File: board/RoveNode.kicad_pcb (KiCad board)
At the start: 4 copper layers, 25.4 x 61 mm, 60 parts, among them J1 Conn_01x05, J3 Conn_01x24_Pin, J4 Conn_01x24_Pin, SW1 RST_Push, SW2 BOOT_Push, U1 STM32H563RITx, U2 AP63203WU-7, U3 SN65HVD232, U4 LAN8742A, U5 USBLC6-4SC6, X1 NX2016SA-25.000M-STD-CZS-1

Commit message: Layout Complete
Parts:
- C1, C10, C11, C13, C14, C15, C16, C19, C20, C3, C30, C31, C32, C33, C34, C35, C4, C7, C8, C9, FB1, R16, R23: moved to B.Cu
- J1: footprint Connector_PinSocket_2.54mm:PinSocket_1x05_P2.54mm_Vertical -> Connector_JST:JST_PH_S5B-PH-K_1x05_P2.00mm_Horizontal
- moved D3 85.4 mm to (123.2, 65.0)
- moved C7 84.4 mm to (131.1, 87.4), turned to 180 degrees
- moved C8 84.2 mm to (131.1, 89.5), turned to 180 degrees
- moved C13 84.1 mm to (127.8, 76.2)
- moved C4 84.0 mm to (127.8, 70.1), turned to 180 degrees
- moved C19 83.9 mm to (127.8, 78.2)
- moved C9 83.9 mm to (131.1, 91.4), turned to 180 degrees
- moved C10 83.6 mm to (131.1, 93.5), turned to 180 degrees
- moved C11 83.4 mm to (131.1, 95.5), turned to 180 degrees
- moved C14 83.1 mm to (131.1, 97.5), turned to 180 degrees
- moved C16 82.7 mm to (125.7, 61.5)
- moved R15 82.1 mm to (131.1, 51.3), turned to 90 degrees
- moved C20 79.8 mm to (127.8, 72.1)
- moved C30 79.8 mm to (127.8, 74.2)
- moved C32 76.1 mm to (124.0, 80.3), turned to 180 degrees
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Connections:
- J3 pad 10: PB7 -> PC15
- J3 pad 11: PB8 -> PH0
- J3 pad 12: PC13 -> PH1
- J3 pad 13: PC14 -> PC2
- J3 pad 14: PC15 -> PC3
- J3 pad 15: PH0 -> PA0
- J3 pad 16: PH1 -> PA3
- J3 pad 17: PC2 -> PA4
- J3 pad 18: PC3 -> PA6
- J3 pad 19: PA0 -> PB0
- J3 pad 2: PA15 -> PD2
- J3 pad 20: PA3 -> PB1
- J3 pad 21: PA4 -> PB2
- J3 pad 22: PA6 -> PB10
- J3 pad 3: PC10 -> PB4
- J3 pad 4: PC11 -> PB5
- J3 pad 5: PC12 -> PB6
- J3 pad 6: PD2 -> PB7
- J3 pad 7: PB4 -> PB8
- J3 pad 8: PB5 -> PC13
- J3 pad 9: PB6 -> PC14
- J4 pad 10: PC8 -> PA10
- J4 pad 11: PC7 -> PA9
- J4 pad 12: PC6 -> PA8
- J4 pad 13: TX- -> PC9
- J4 pad 14: PB14 -> PC8
- J4 pad 15: PB13 -> PC7
- J4 pad 16: TX+ -> PC6
- J4 pad 17: PB10 -> PB14
- J4 pad 18: PB2 -> PB13
- J4 pad 19: PB1 -> RX+
- J4 pad 20: PB0 -> RX-
- J4 pad 21: RX- -> TX+
- J4 pad 22: RX+ -> TX-
- J4 pad 23: LED1 -> LED2
- J4 pad 24: LED2 -> LED1
- J4 pad 4: CAN_H -> CAN_L
- J4 pad 5: CAN_L -> CAN_H
- J4 pad 6: PA10 -> PC12
- J4 pad 7: PA9 -> PC11
- J4 pad 8: PA8 -> PC10
- J4 pad 9: PC9 -> PA15
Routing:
- net VIN: track 0.00 -> 82.5 mm, vias 0 -> 3
- net GND: track 7.94 -> 62.9 mm, vias 6 -> 80
- net PD2: track 0.00 -> 39.2 mm, vias 0 -> 1
- net SWDIO: track 0.00 -> 36.4 mm, vias 0 -> 1
- net CAN_TX: track 0.00 -> 35.3 mm, vias 0 -> 2
- net PB4: track 0.00 -> 34.9 mm, vias 0 -> 1
- net SWDCLK: track 1.49 -> 36.4 mm
- net CAN_RX: track 0.00 -> 34.9 mm, vias 0 -> 2
- net SWO: track 0.00 -> 34.1 mm, vias 0 -> 1
- net LED1: track 0.00 -> 33.8 mm
- net PB5: track 0.00 -> 31.5 mm, vias 0 -> 1
- net RX+: track 2.59 -> 33.8 mm, vias 0 -> 2
- net ETH_REF_CLK: track 11.7 -> 41.7 mm, vias 2 -> 1
- net TX-: track 5.47 -> 34.8 mm, vias 0 -> 2
- net RX-: track 5.13 -> 33.6 mm, vias 2 -> 3
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- added copper zone on B.Cu, net +3V3
- added copper zone on F.Cu, net Net-(U2-SW)
- added copper zone on B.Cu, net Net-(U4-VDD1A)
- added copper zone on F.Cu, net VIN

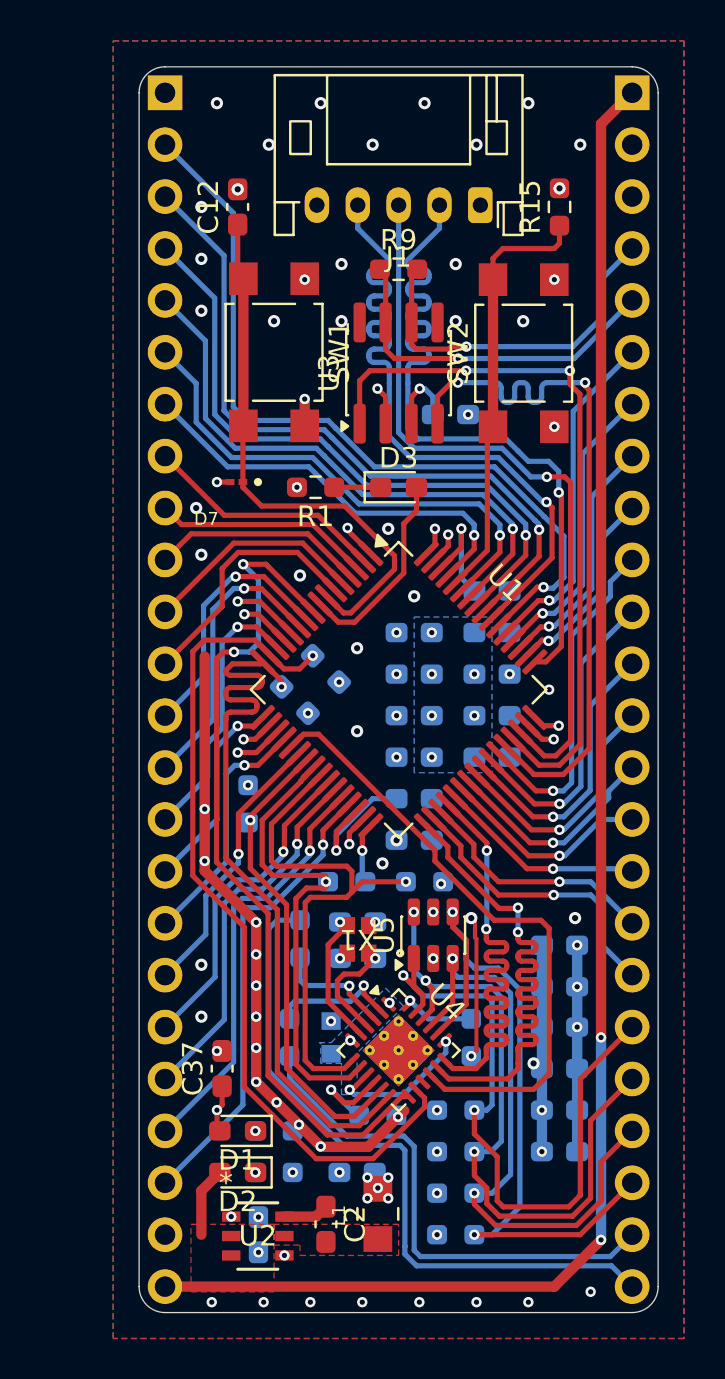
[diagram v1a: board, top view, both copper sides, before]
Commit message: Replaced buck with AP2303, fixed PHY schematic
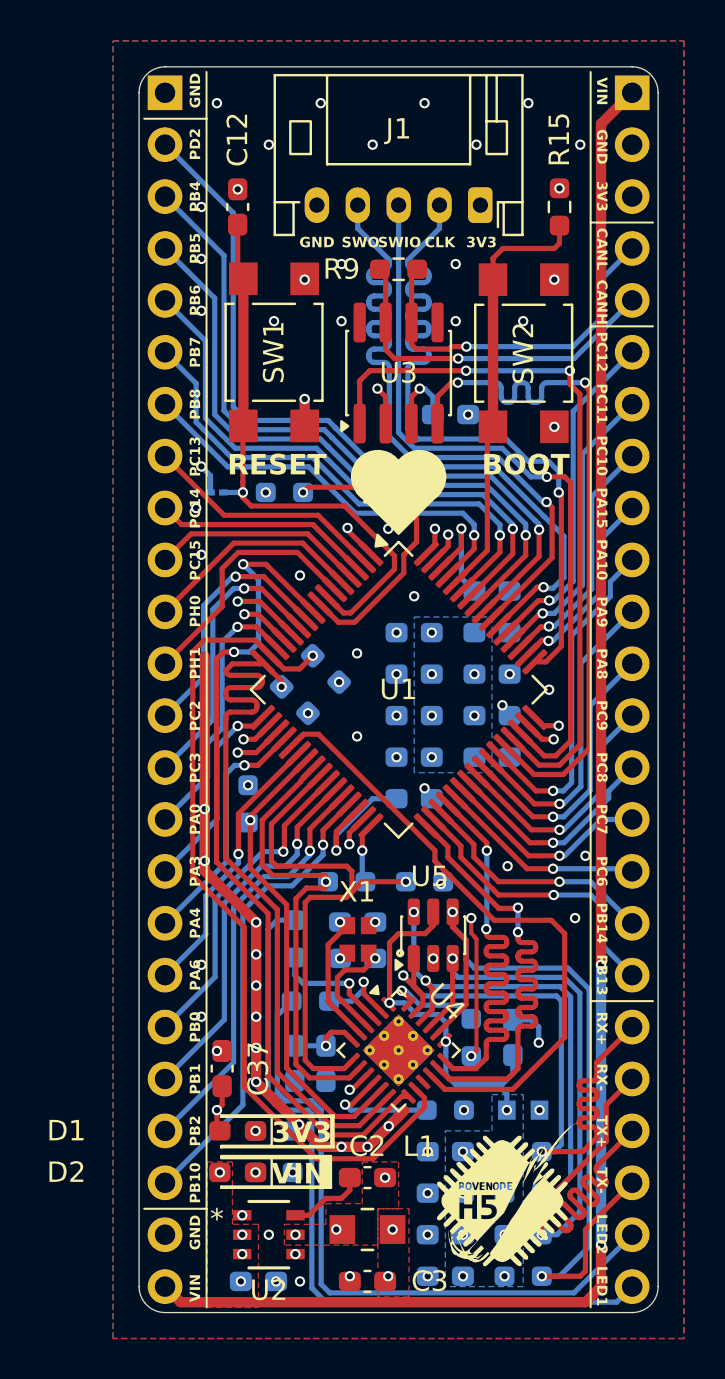
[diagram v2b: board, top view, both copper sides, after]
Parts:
- added G***: LOGO, LOGO, F.Cu at (128.8, 99.6)
- added G***: LOGO, LOGO, B.Cu at (123.2, 49.0)
- added G***: LOGO, LOGO, B.Cu at (123.2, 65.8)
- C3: moved to F.Cu
- D7, R1: moved to B.Cu
- moved C11 13.2 mm to (118.1, 93.2), turned to -90 degrees
- moved C9 11.6 mm to (125.5, 101.6)
- moved C7 11.5 mm to (125.5, 97.5)
- moved C8 11.5 mm to (125.5, 99.6)
- moved C10 11.4 mm to (119.6, 93.2), turned to -90 degrees
- moved C15 10.8 mm to (128.8, 91.9), turned to 90 degrees
- moved FB1 10.0 mm to (129.3, 95.5), turned to 180 degrees
- moved C14 8.27 mm to (125.5, 103.6)
- moved C3 5.36 mm to (121.7, 103.9)
- moved R11 3.88 mm to (129.3, 103.6)
- moved R10 3.88 mm to (129.3, 101.6)
- moved R12 3.88 mm to (129.3, 97.5)
- moved R13 3.88 mm to (129.3, 99.6)
- moved R7 3.31 mm to (125.5, 95.5)
- moved C2 3.06 mm to (121.7, 98.8), turned to 0 degrees
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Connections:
- C10 pad 1: +3V3 -> Net-(U4-VDDCR)
- C11 pad 1: +3V3 -> Net-(U4-VDDCR)
- C14 pad 1: +3V3 -> Net-(U4-VDD1A)
- C15 pad 1: +3V3 -> Net-(U4-VDD1A)
- C7 pad 1: +3V3 -> Net-(U4-VDD1A)
- C8 pad 1: +3V3 -> Net-(U4-VDD1A)
- C9 pad 1: +3V3 -> Net-(U4-VDD1A)
- R10 pad 1: +3V3 -> Net-(U4-VDD1A)
- R11 pad 1: +3V3 -> Net-(U4-VDD1A)
- R12 pad 1: +3V3 -> Net-(U4-VDD1A)
- R13 pad 1: +3V3 -> Net-(U4-VDD1A)
- U4 pad 6: Net-(U4-VDD1A) -> Net-(U4-VDDCR)
- U4 pad 9: Net-(U4-VDD1A) -> +3V3
- U5 pad 5: +3V3 -> Net-(U4-VDD1A)
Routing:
- net Net-(U4-VDD1A): track 7.68 -> 18.0 mm, vias 4 -> 11
- net TX+: track 30.4 -> 38.9 mm
- net LED2: track 24.9 -> 32.4 mm
- net GND: track 62.9 -> 55.8 mm
- net TX-: track 34.8 -> 39.0 mm
- net Net-(U4-VDDCR): track 0.00 -> 3.50 mm, vias 0 -> 1
- net LED1: track 33.8 -> 37.0 mm
- net Net-(U4-LED2/~{INTSEL}): track 6.37 -> 4.11 mm
- net RX-: track 33.6 -> 31.6 mm
- net Net-(D3-K): track 2.28 -> 3.91 mm, vias 0 -> 1
- net Net-(U2-BST): track 2.23 -> 3.78 mm
- net TX_D0: track 27.2 -> 25.7 mm
- net VIN: track 82.5 -> 81.0 mm, vias 3 -> 6
- net Net-(U4-RXER/PHYAD0): track 4.70 -> 5.99 mm
- net NRST: track 26.9 -> 28.2 mm, vias 0 -> 1
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- added copper zone on F.Cu, net +3V3
- added copper zone on In2.Cu, net GND
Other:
- board text added: "3V3"
- board text added: "BOOT"
- board text added: "CANH"
- board text added: "CANL"
- board text added: "CLK"
- board text added: "GND"
- board text added: "LED1"
- board text added: "LED2"
- board text added: "PA0"
- board text added: "PA10"
- board text added: "PA15"
- board text added: "PA3"
- board text added: "PA4"
- board text added: "PA6"
- board text added: "PA8"
- board text added: "PA9"
- board text added: "PB0"
- board text added: "PB1"
- board text added: "PB10"
- board text added: "PB13"
- board text added: "PB14"
- board text added: "PB2"
- board text added: "PB4"
- board text added: "PB5"
- board text added: "PB6"
- board text added: "PB7"
- board text added: "PB8"
- board text added: "PC10"
- board text added: "PC11"
- board text added: "PC12"
- board text added: "PC13"
- board text added: "PC14"
- board text added: "PC15"
- board text added: "PC2"
- board text added: "PC3"
- board text added: "PC6"
- board text added: "PC7"
- board text added: "PC8"
- board text added: "PC9"
- board text added: "PD2"
- board text added: "PH0"
- board text added: "PH1"
- board text added: "RESET"
- board text added: "RX+"
- board text added: "RX-"
- board text added: "RoveNode - H5.1.1 Mars Rover Design Team Missouri S&T 2027 Will Grove"
- board text added: "SWIO"
- board text added: "SWO"
- board text added: "TX+"
- board text added: "TX-"
- board text added: "VIN"

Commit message: Board Ordered
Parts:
- removed D7: ESDALC6V1-1U2, SignalStack:DIODE_ESDALC6V1-1U2
- added D4: D_TVS, Diode_SMD:D_0603_1608Metric_Pad1.05x0.95mm_HandSolder, B.Cu at (114.6, 66.2)
- moved C2 1.02 mm to (121.7, 99.8)
- moved C37 0.76 mm to (114.6, 94.2)
- moved D1 0.51 mm to (115.3, 97.0)
- moved R23 0.51 mm to (117.1, 97.0)
- moved L1 0.51 mm to (121.7, 101.9)
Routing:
- net RX+: track 34.0 -> 31.6 mm
- net GND: track 55.8 -> 57.3 mm, vias 80 -> 87
- net +3V3: track 29.5 -> 30.8 mm, vias 25 -> 27
- net TX_EN: track 31.0 -> 32.0 mm
- net Net-(U2-BST): track 3.78 -> 3.00 mm
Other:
- board text added: "CAN"
- board text added: "Ethernet"
- board text added: "Flashes"
- board text added: "Power"
- board text added: "S/N"
- board text added: "Unpow"

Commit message: Schematic and Layout Complete
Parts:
- removed the G*** at (128.8, 99.6)
- removed the G*** at (123.2, 49.0)
- removed the G*** at (123.2, 65.8)
- added D5: D_TVS, Diode_SMD:D_SMA, B.Cu at (120.3, 100.1)
- added D6: D_Schottky, Diode_SMD:D_SOD-123F, B.Cu at (115.8, 101.1)
- added F1: 2A, Fuse:Fuse_1206_3216Metric_Pad1.42x1.75mm_HandSolder, B.Cu at (116.1, 103.5)
- added G***: LOGO, LOGO, F.Cu at (128.5, 100.1)
- added G***: LOGO, LOGO, B.Cu at (123.2, 47.8)
- added G***: LOGO, LOGO, B.Cu at (117.3, 71.9)
- added R18: 10K, Resistor_SMD:R_0603_1608Metric_Pad0.98x0.95mm_HandSolder, B.Cu at (130.0, 86.7)
- added R19: 0, Resistor_SMD:R_0603_1608Metric_Pad0.98x0.95mm_HandSolder, B.Cu at (131.8, 86.7)
- added R20: 10k, Resistor_SMD:R_0603_1608Metric_Pad0.98x0.95mm_HandSolder, B.Cu at (119.1, 89.0)
- added R21: 10k, Resistor_SMD:R_0603_1608Metric_Pad0.98x0.95mm_HandSolder, B.Cu at (119.3, 86.4)
- C12, C2, C3, C37, R15: moved to B.Cu
- D3: value BLUE -> RED
- L1: footprint SignalStack:INDM2520X190N -> Inductor_SMD:L_1812_4532Metric_Pad1.30x3.40mm_HandSolder; moved to B.Cu
- R1: value 330 -> 150
- R5: value 10K -> 1k5
- moved C12 24.6 mm to (125.1, 73.9), turned to -90 degrees
- moved R15 22.6 mm to (129.7, 73.9), turned to -90 degrees
- moved D4 14.3 mm to (126.6, 73.9)
- moved R1 13.6 mm to (128.1, 73.9), turned to -90 degrees
- moved C9 10.7 mm to (130.0, 91.9), turned to 90 degrees
- moved C37 9.89 mm to (123.4, 98.6)
- moved C3 9.11 mm to (130.7, 102.6), turned to 0 degrees
- moved C14 8.65 mm to (126.0, 95.0)
- moved C34 8.46 mm to (125.1, 80.5), turned to -90 degrees
- moved C16 7.90 mm to (125.1, 69.3), turned to -90 degrees
- moved C35 6.89 mm to (126.6, 80.5), turned to -90 degrees
- moved R6 6.65 mm to (118.9, 80.5), turned to -90 degrees
- moved U2 6.40 mm to (123.2, 100.8)
- moved C33 6.16 mm to (129.7, 80.5), turned to -90 degrees
- moved C31 6.02 mm to (128.1, 80.5), turned to -90 degrees
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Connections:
- C1 pad 1: VIN -> Net-(D2-A)
- D2 pad 2: VIN -> Net-(D2-A)
- U2 pad 2: VIN -> Net-(D2-A)
- U2 pad 3: VIN -> Net-(D2-A)
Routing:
- net /Ethernet PHY/NRST: track 0.00 -> 16.2 mm, vias 0 -> 1
- net +3V3: track 30.8 -> 40.9 mm, vias 27 -> 32
- net Net-(D3-K): track 3.91 -> 12.6 mm
- net TX+: track 38.9 -> 31.4 mm
- net TX-: track 39.0 -> 31.8 mm
- net Net-(U2-SW): track 0.00 -> 5.82 mm, vias 3 -> 1
- net NRST: track 28.3 -> 34.0 mm
- net GND: track 57.3 -> 51.5 mm, vias 87 -> 94
- net MDIO: track 36.7 -> 41.8 mm
- net Net-(U4-VDD1A): track 18.0 -> 13.2 mm, vias 11 -> 2
- net ETH_REF_CLK: track 41.7 -> 46.2 mm
- net VCAP: track 12.4 -> 7.93 mm
- net RX-: track 31.6 -> 28.0 mm
- net Net-(U4-RXER/PHYAD0): track 5.99 -> 2.44 mm
- net RX+: track 31.6 -> 29.3 mm
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- added copper zone on B.Cu, net Net-(D2-A)
- added copper zone on B.Cu, net Net-(D6-A)
- added copper zone on B.Cu, net Net-(U2-SW)
- added copper zone on B.Cu, net VIN
- removed copper zone on F.Cu, net +3V3
- removed copper zone on F.Cu, net Net-(U2-SW)
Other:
- board text added: "RoveNode - H5.1.2 Mars Rover Design Team Missouri S&T 2027 Will Grove"
- board text removed: "CAN"
- board text removed: "Ethernet"
- board text removed: "Flashes"
- board text removed: "Power"
- board text removed: "RoveNode - H5.1.1 Mars Rover Design Team Missouri S&T 2027 Will Grove"
- board text removed: "S/N"
- board text removed: "Unpow"
